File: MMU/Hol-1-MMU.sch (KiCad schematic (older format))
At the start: 25 parts, among them P1 DATA BUS, P2 ADDRESS PORT, P3 DATA PORT, P4 MMU CONTROL, SW1 HEX_SWITCH, SW2 HEX_SWITCH, SW3 HEX_SWITCH, SW4 HEX_SWITCH, SW5 SPDT, SW6 SW_PUSH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

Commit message: v1.5.1 MMU component footprints created
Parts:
- P2: footprint ~ -> (none)
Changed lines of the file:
@@
 Sheet 1 1
 Title "Hol-1 8-bit CPU - Memory Management Unit"
-Date "4 jul 2019"
+Date "13 jul 2019"
 Rev "1"
 Comp "www.benningtons.net"
@@
 F 0 "P2" V 9000 3550 60  0000 C CNN
 F 1 "ADDRESS PORT" V 9100 3550 60  0000 C CNN
-F 2 "~" H 9050 3550 60  0000 C CNN
+F 2 "" H 9050 3550 60  0000 C CNN
 F 3 "~" H 9050 3550 60  0000 C CNN
 	1    9050 3550

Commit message: v1.5.2 MMU power + blinkenlights added
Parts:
- removed SW5: SPDT, ~, symbol SPDT
- added JP1, JP2: Blinkenlights, ~, symbol 9-PIN_HEADER
- added P5: Power, ~, symbol CONN_2
- added SW5: DPDT, ~, symbol DPDT
- R1: value R -> 220Ω
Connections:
- wire segments 192 -> 202
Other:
- note added: "In Program mode use SW6\nto load selected RAM address\nwith data from Data Output port"
- note removed: "In Program mode use SW?\nto load selected RAM address\nwith data from Data Output port"
- moved on the sheet: U2, U4

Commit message: v1.5.3 initial MMU board layout
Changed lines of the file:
@@
 Sheet 1 1
 Title "Hol-1 8-bit CPU - Memory Management Unit"
-Date "27 jul 2019"
+Date "28 jul 2019"
 Rev "1"
 Comp "www.benningtons.net"
@@
 	-1   0    0    1
 $EndComp
-Text Label 7400 5700 0    60   ~ 0
+Text Label 7400 5300 0    60   ~ 0
 CLK
 Text Label 7400 5200 0    60   ~ 0
 IN-D
-Text Label 7400 5800 0    60   ~ 0
+Text Label 7400 5500 0    60   ~ 0
 RAM-INPUT
 Text Label 7400 5100 0    60   ~ 0
@@
 6-bit memory addressing\nso top 2 bits ignored
 NoConn ~ 7400 5600
-NoConn ~ 7400 5300
-NoConn ~ 7400 5500
+NoConn ~ 7400 5800
+NoConn ~ 7400 5700
 NoConn ~ 7400 5400
 Text Notes 650  7400 0    60   ~ 0
@@
 	8875 6300 8350 6300
 Wire Wire Line
-	8875 6200 8350 6200
+	8350 6200 8875 6200
 Wire Wire Line
 	10750 5750 11100 5750
@@
 	7400 5200 7650 5200
 Wire Wire Line
-	7400 5700 7600 5700
-Wire Wire Line
-	7400 5800 8350 5800
-Wire Wire Line
-	8350 5800 8350 6200
+	8350 5500 8350 6200
 Wire Wire Line
 	7400 5100 7800 5100
@@
 Wire Wire Line
 	6800 850  6800 1000
+Wire Wire Line
+	7400 5300 7650 5300
+Wire Wire Line
+	7400 5500 8350 5500
 $EndSCHEMATC

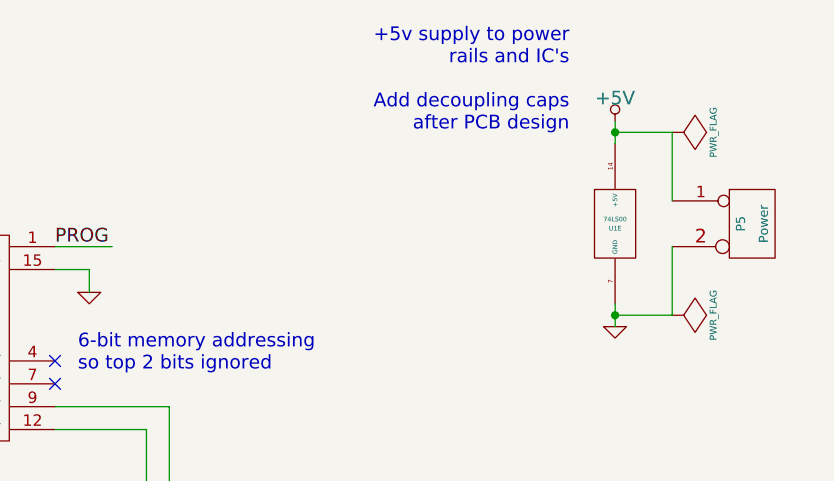
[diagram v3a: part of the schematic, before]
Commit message: v1.5.4 MMU add bypass caps
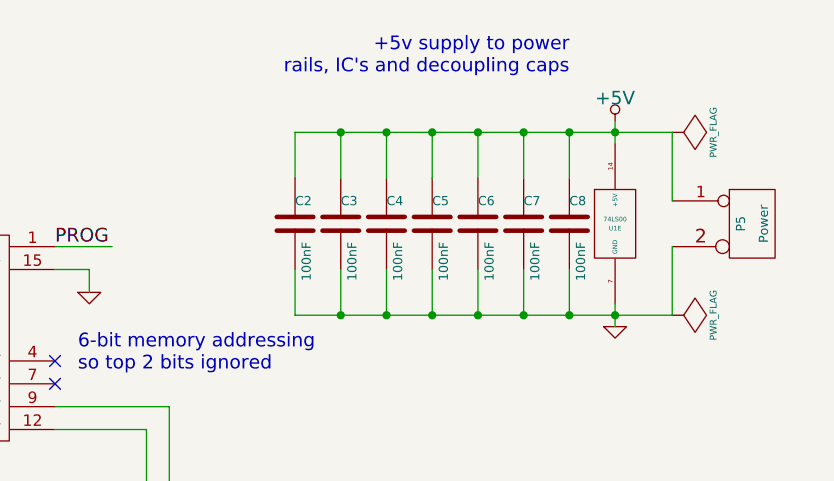
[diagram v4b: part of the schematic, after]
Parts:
- added C2, C3, C4, C5, C6, C7, C8: 100nF, ~, symbol C
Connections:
- wire segments 202 -> 216
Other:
- note added: "+5v supply to power\nrails, IC's and decoupling caps\n"
- note removed: "+5v supply to power\nrails and IC's\n\nAdd decoupling caps\nafter PCB design"

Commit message: v1.5.6 MMU 10-pin jumpers for hex display blinkenlights
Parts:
- removed JP1, JP2: Blinkenlights, ~, symbol 9-PIN_HEADER
- added JP1, JP2: Blinkenlights, ~, symbol 10-PIN_HEADER
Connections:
- wire segments 216 -> 215
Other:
- moved on the sheet: SW1, SW2, SW3, SW4, U2, U4

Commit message: v1.5.8 MMU added blinkenlights to display memory address register
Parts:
- added JP3: Blinkenlights, ~, symbol 9-PIN_HEADER
- JP1, JP2: value Blinkenlights -> Blinken hex lights
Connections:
- wire segments 215 -> 216
- no-connect marks 15 -> 25
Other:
- moved on the sheet: C1, C2, C3, C4, C5, C6, C7, C8, D1, D2, JP1, P2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

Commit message: v1.5.9 MMU tie unused inputs to ground
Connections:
- wire segments 216 -> 232
- no-connect marks 25 -> 13
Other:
- note added: "Register D (address register)\nupper 4-bits (U2)\nlower 4-bits (U4)"
- note removed: "Register D (address register)\nupper 4-bits (U?)\nlower 4-bits (U?)"
- moved on the sheet: P2, U3, U5

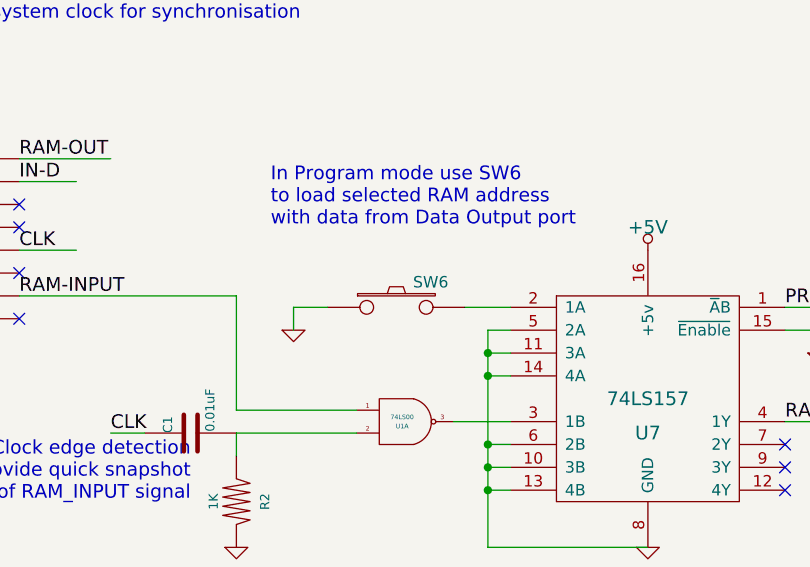
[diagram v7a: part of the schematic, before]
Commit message: v1.5.13 MMU: adjustments during construction
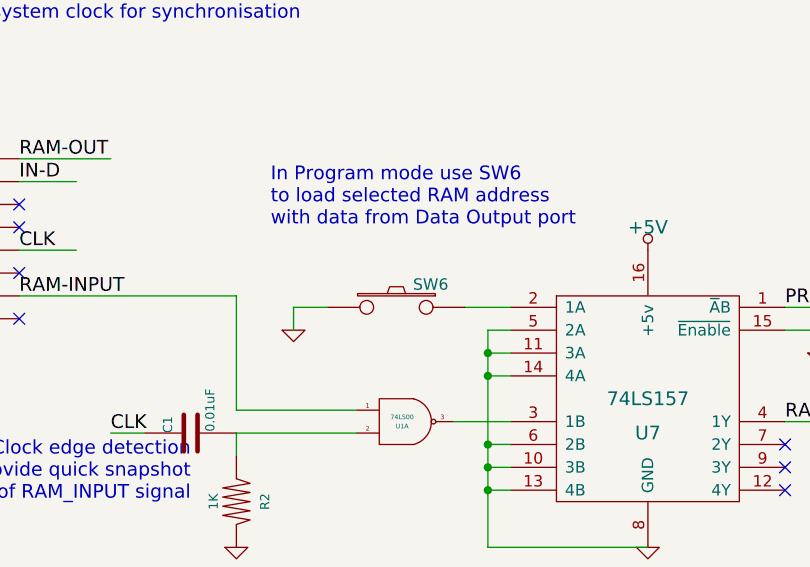
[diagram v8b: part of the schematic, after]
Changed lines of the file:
@@
 Sheet 1 1
 Title "Hol-1 8-bit CPU - Memory Management Unit"
-Date "2 aug 2019"
+Date "8 sep 2019"
 Rev "1"
 Comp "www.benningtons.net"
@@
 U 1 1 5D102E6A
 P 9100 5950
-F 0 "SW6" H 9250 6060 50  0000 C CNN
+F 0 "SW6" H 8950 6050 50  0000 C CNN
 F 1 "SW_PUSH" H 9100 5870 50  0001 C CNN
 F 2 "~" H 9100 5950 60  0000 C CNN
 F 3 "~" H 9100 5950 60  0000 C CNN
 	1    9100 5950
-	1    0    0    -1
-$EndComp
-$Comp
+	-1   0    0    -1
+$EndComp
+$Comp
